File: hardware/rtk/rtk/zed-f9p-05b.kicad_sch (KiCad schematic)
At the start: 3 parts, among them J5 Conn_Coaxial, U4 ZED-F9H-01B

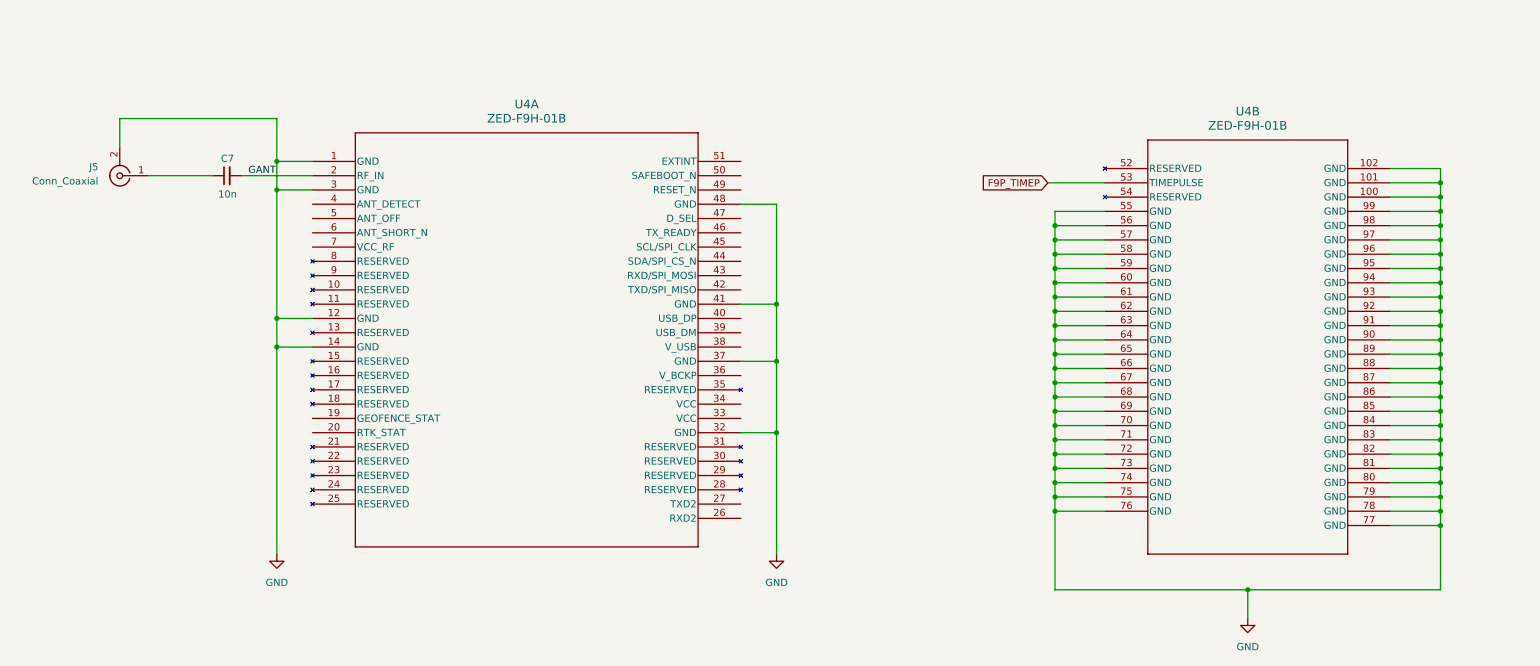
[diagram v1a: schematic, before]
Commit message: Schematic progress: all sheets ~90% complete (#182)
- power.kicad_sch: PSU, BQ24075, LiPo connector, USB-C power path
- stm32f765vit.kicad_sch: F765VIT pin assignments, SPI2/I2C4/SDMMC1/UART7/8/USART3
- usb2hs.kicad_sch: USB3300 ULPI, 24MHz TCXO (ASTX-H11-24MHz), USB-C connector, diff pair nets USB_D+/USB_D-
- zed-f9p-05b.kicad_sch: ZED-F9P-05B connections
- rtk-base.ioc: DIO1 corrected to GPIO_Input, LSM6DSOX CS removed (I2C mode, CS tied high in schematic), DIO2 label typo fixed
- rtk.kicad_pcb/pro: project settings updated

Co-Authored-By: Claude Sonnet 4.6 <noreply@anthropic.com>
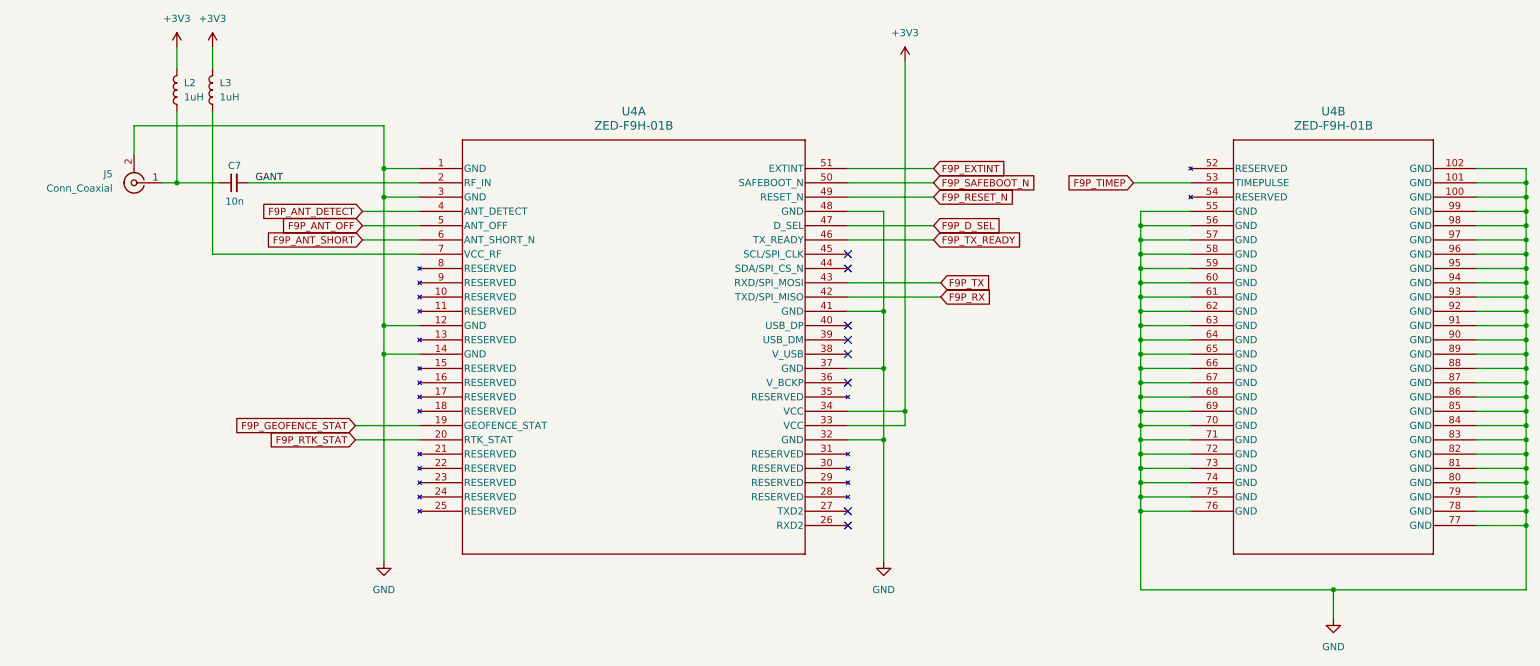
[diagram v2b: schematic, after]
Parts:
- added L2, L3: 1uH, DFE201610E-1R0M-P2:IND_DFE2016_2X1P6_MUR, symbol Device:L
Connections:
- net at C7.1, J5.1 (In): now also L2.1
- net F9P_GEOFENCE_STAT: now reaches U4.19 (GEOFENCE_STAT)
- net F9P_RTK_STAT: now reaches U4.20 (RTK_STAT)
- net +3V3: now reaches U4.33 (VCC)
- net +3V3: now also U4.34 (VCC), L2.2, L3.2
- net F9P_ANT_DETECT: now reaches U4.4 (ANT_DETECT)
- net F9P_RX: now reaches U4.42 (TXD/SPI_MISO)
- net F9P_TX: now reaches U4.43 (RXD/SPI_MOSI)
- net F9P_TX_READY: now reaches U4.46 (TX_READY)
- net F9P_D_SEL: now reaches U4.47 (D_SEL)
- net F9P_RESET_N: now reaches U4.49 (RESET_N)
- net F9P_ANT_OFF: now reaches U4.5 (ANT_OFF)
- net F9P_SAFEBOOT_N: now reaches U4.50 (SAFEBOOT_N)
- net F9P_EXTINT: now reaches U4.51 (EXTINT)
- net F9P_ANT_SHORT: now reaches U4.6 (ANT_SHORT_N)
- net at U4.7 (VCC_RF): now also L3.1
- no-connect marks 0 -> 8
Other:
- moved on the sheet: C7, J5, U4A, U4B

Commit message: ZED-F9P sheet review fixes (#182)
- V_BCKP tied to +3V3 with 100nF decoupling
- VCC decoupling caps added on module side of L2/L3
- SAFEBOOT_N and RESET_N 10k pull-ups to +3V3 added
- L3 on VCC_RF replaced with ferrite bead (600R at 100MHz)

Co-Authored-By: Claude Sonnet 4.6 <noreply@anthropic.com>
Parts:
- removed L2, L3: 1uH, DFE201610E-1R0M-P2:IND_DFE2016_2X1P6_MUR, symbol Device:L
- added C34: 100n, Capacitor_SMD:C_0603_1608Metric_Pad1.08x0.95mm_HandSolder, symbol Device:C_Small
- added FB1, FB2: FerriteBead_Small, Capacitor_SMD:C_0805_2012Metric_Pad1.18x1.45mm_HandSolder, symbol Device:FerriteBead_Small
- added R18, R19: 10k, Resistor_SMD:R_0805_2012Metric_Pad1.20x1.40mm_HandSolder, symbol Device:R
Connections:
- net +3V3: now also U4.36 (V_BCKP), C34.2, FB1.1, FB2.1, R18.2, R19.2
- net F9P_RESET_N: now also R19.1
- net F9P_SAFEBOOT_N: now also R18.1
- net GND: now also C34.1
- net at U4.7 (VCC_RF): now also FB2.2
- net at C7.1, J5.1 (In): now also FB1.2
- no-connect marks 8 -> 7
